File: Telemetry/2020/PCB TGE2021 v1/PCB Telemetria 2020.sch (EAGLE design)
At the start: 39 parts, among them IC1 INA240A1DR, IC2 MCP3221A6T-E_OTVAO, IC3 AZ1117IH-3.3TRG1, IC4 ACS758LCB-050B-PFF-T, IC5 ADS1115IDGSR, IC7 ACS758LCB-050B-PFF-T

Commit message: corrigindo esquematico
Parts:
- removed C13: 360pF, rcl:C-USC0805
- removed C14, C15: 100nF, rcl:C-USC0805
- removed IC7: ACS758LCB-050B-PFF-T, allegro:ACS758LCB-050B-PFF-T
- removed R10: 47k, rcl:R-US_R0805
- removed R15: 4.7k, rcl:R-US_R0805
- removed R9: 160k, rcl:R-US_R0805
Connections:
- removed net HS_OUT: IC7.VOUT, R15.1
- removed net HS_OUTF: C15.1, R15.2
- removed net PS_AIN4: C13.1, R10.1, R9.2
- net GND: no longer C13.2, C14.2, C15.2, IC7.GND, IC7.IP-, R10.2
- net VCC_12V: no longer IC7.IP+, R9.1
- net VCC_3V3: no longer C14.1, IC7.VCC
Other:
- note removed: "12V Power Supply Current Measurement"
- note removed: "12V Power Supply Voltage Measurement"

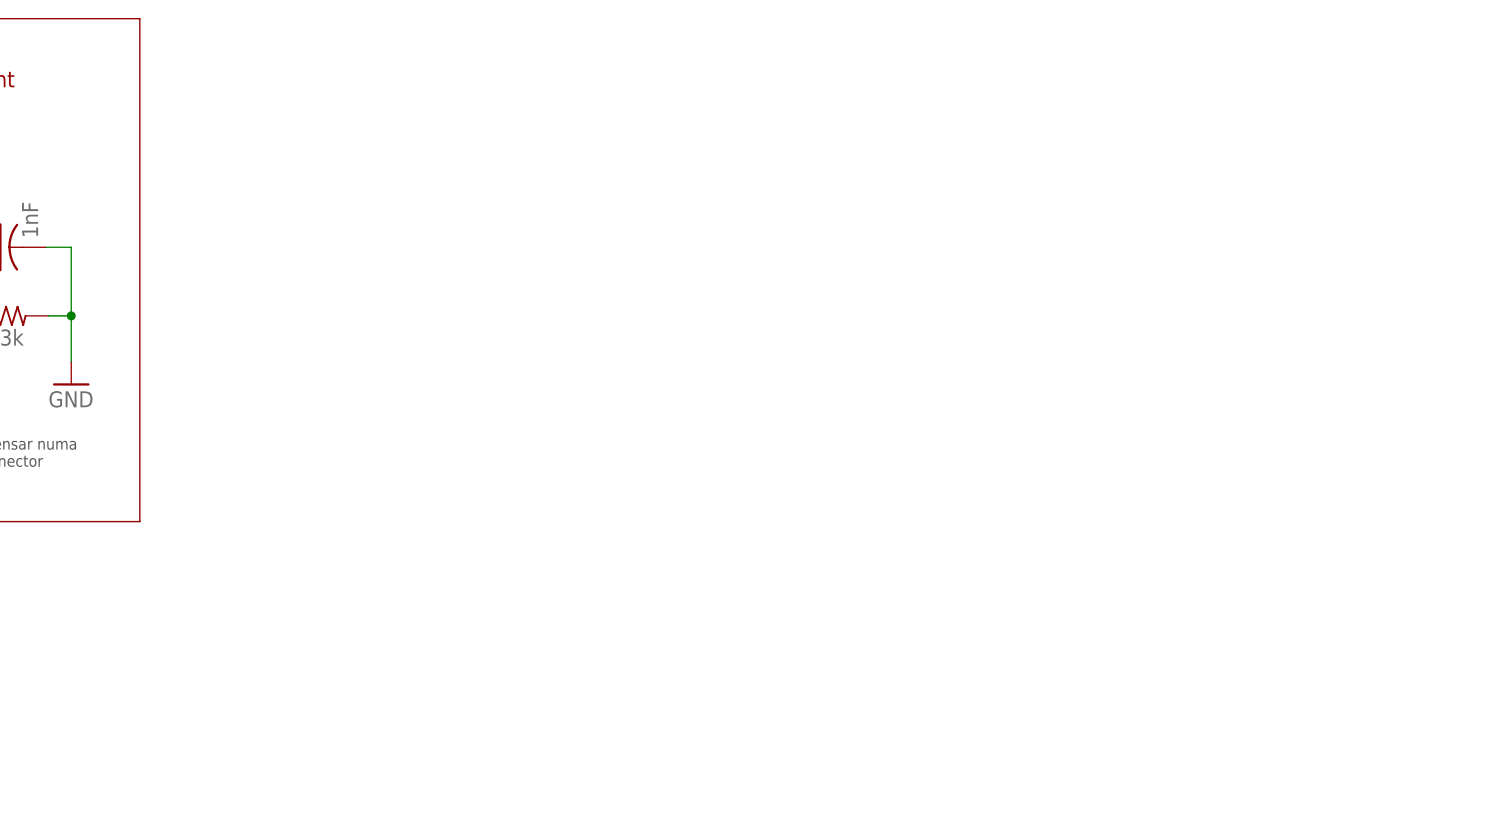
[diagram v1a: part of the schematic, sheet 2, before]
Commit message: Adding voltage and current measurements for the 12V Power Supply
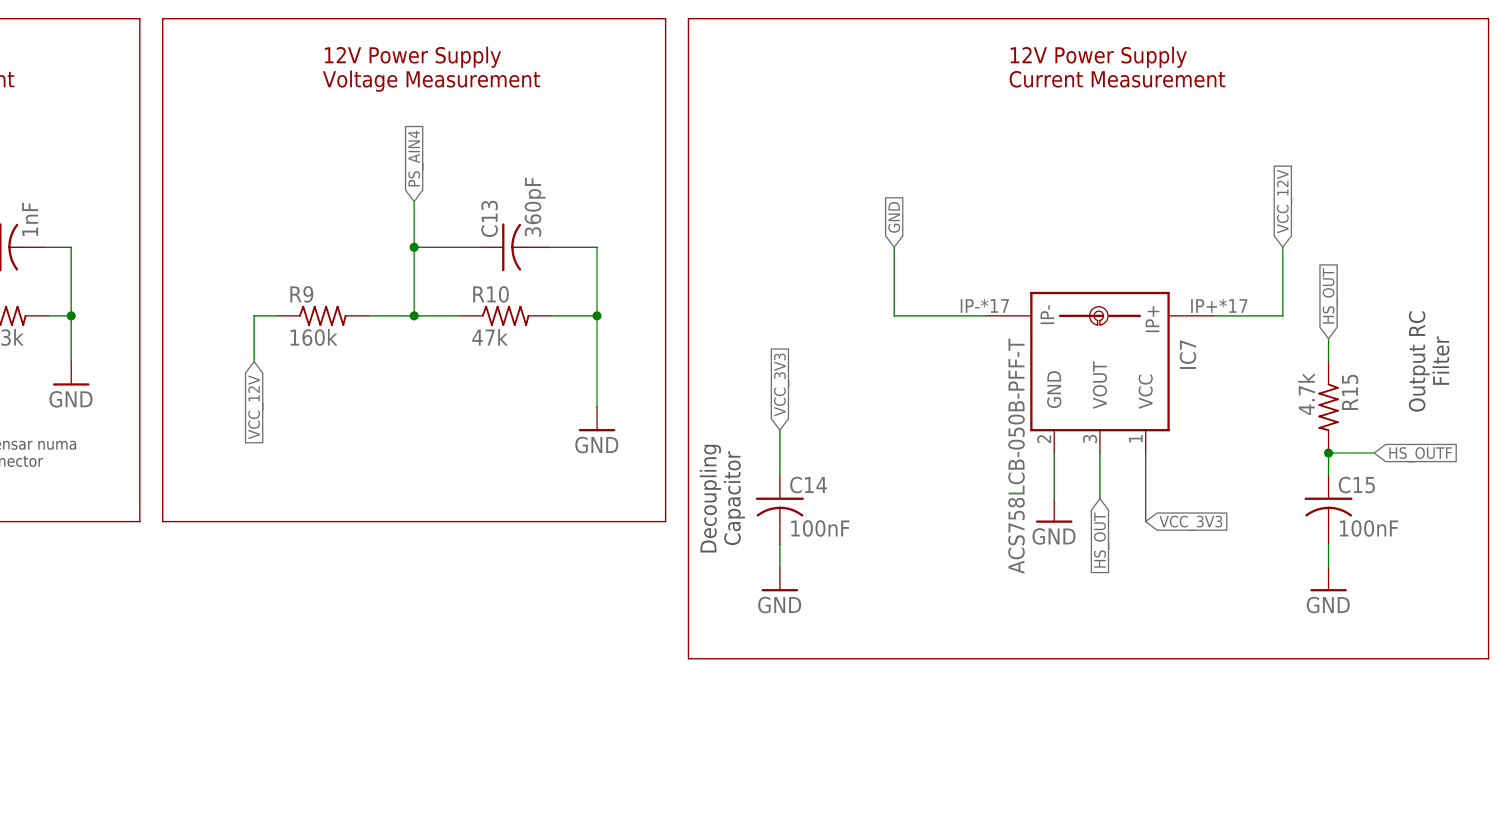
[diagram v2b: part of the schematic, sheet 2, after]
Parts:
- added C13: 360pF, rcl:C-USC0805
- added C14, C15: 100nF, rcl:C-USC0805
- added IC7: ACS758LCB-050B-PFF-T, allegro:ACS758LCB-050B-PFF-T
- added R10: 47k, rcl:R-US_R0805
- added R15: 4.7k, rcl:R-US_R0805
- added R9: 160k, rcl:R-US_R0805
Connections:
- new net HS_OUT: IC7.VOUT, R15.1
- new net HS_OUTF: C15.1, R15.2
- new net PS_AIN4: C13.1, R10.1, R9.2
- net GND: now also C13.2, C14.2, C15.2, IC7.GND, IC7.IP-, R10.2
- net VCC_12V: now also IC7.IP+, R9.1
- net VCC_3V3: now also C14.1, IC7.VCC
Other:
- note added: "12V Power Supply Current Measurement"
- note added: "12V Power Supply Voltage Measurement"
